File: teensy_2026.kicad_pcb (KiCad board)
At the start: 2 copper layers, 24.5 x 18 mm, 0 parts

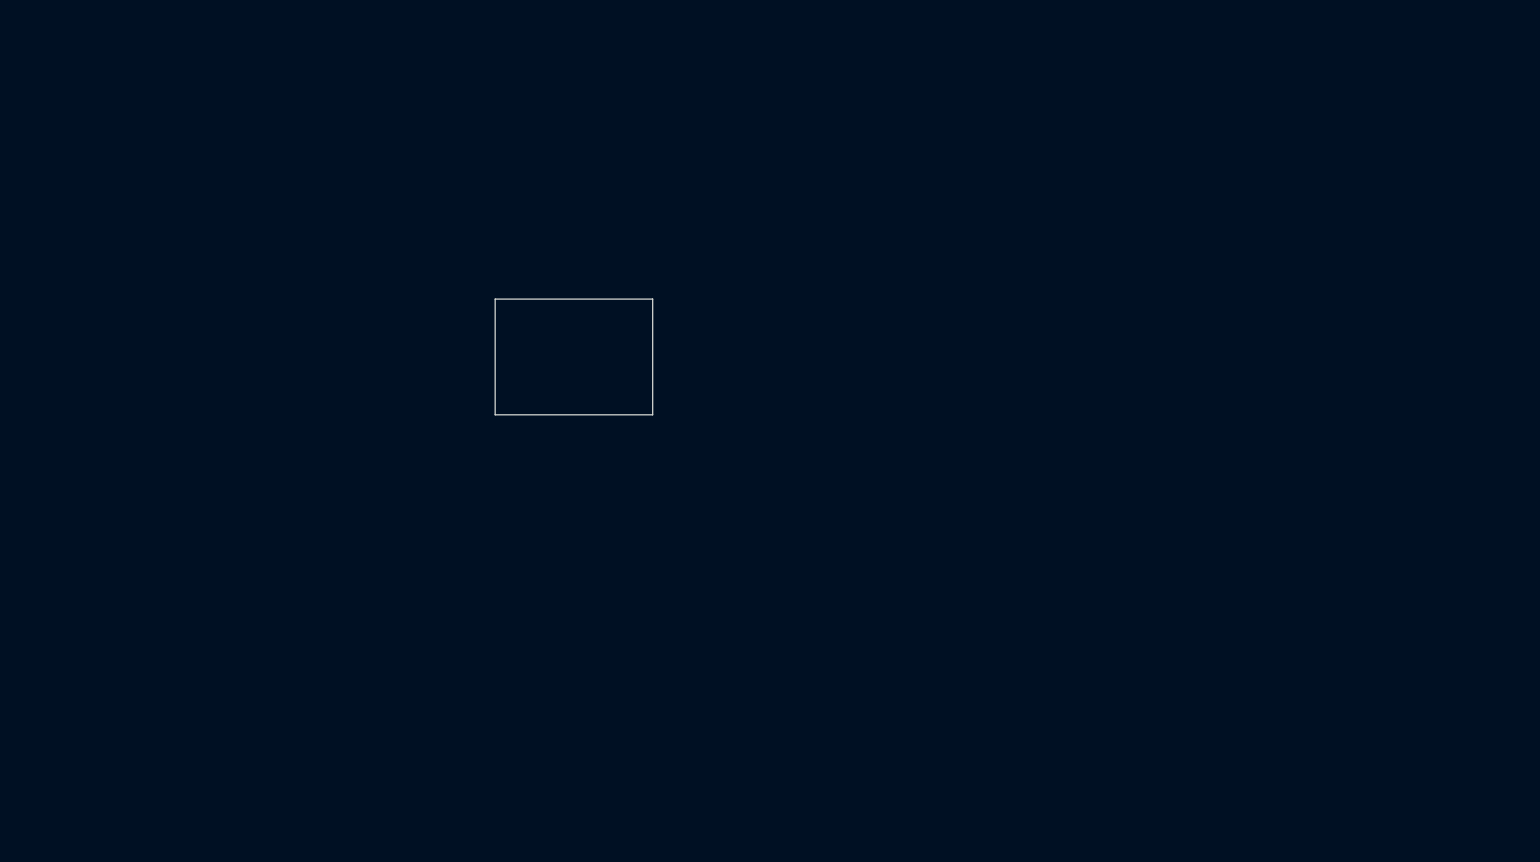
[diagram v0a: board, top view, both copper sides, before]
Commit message: started pcb layout
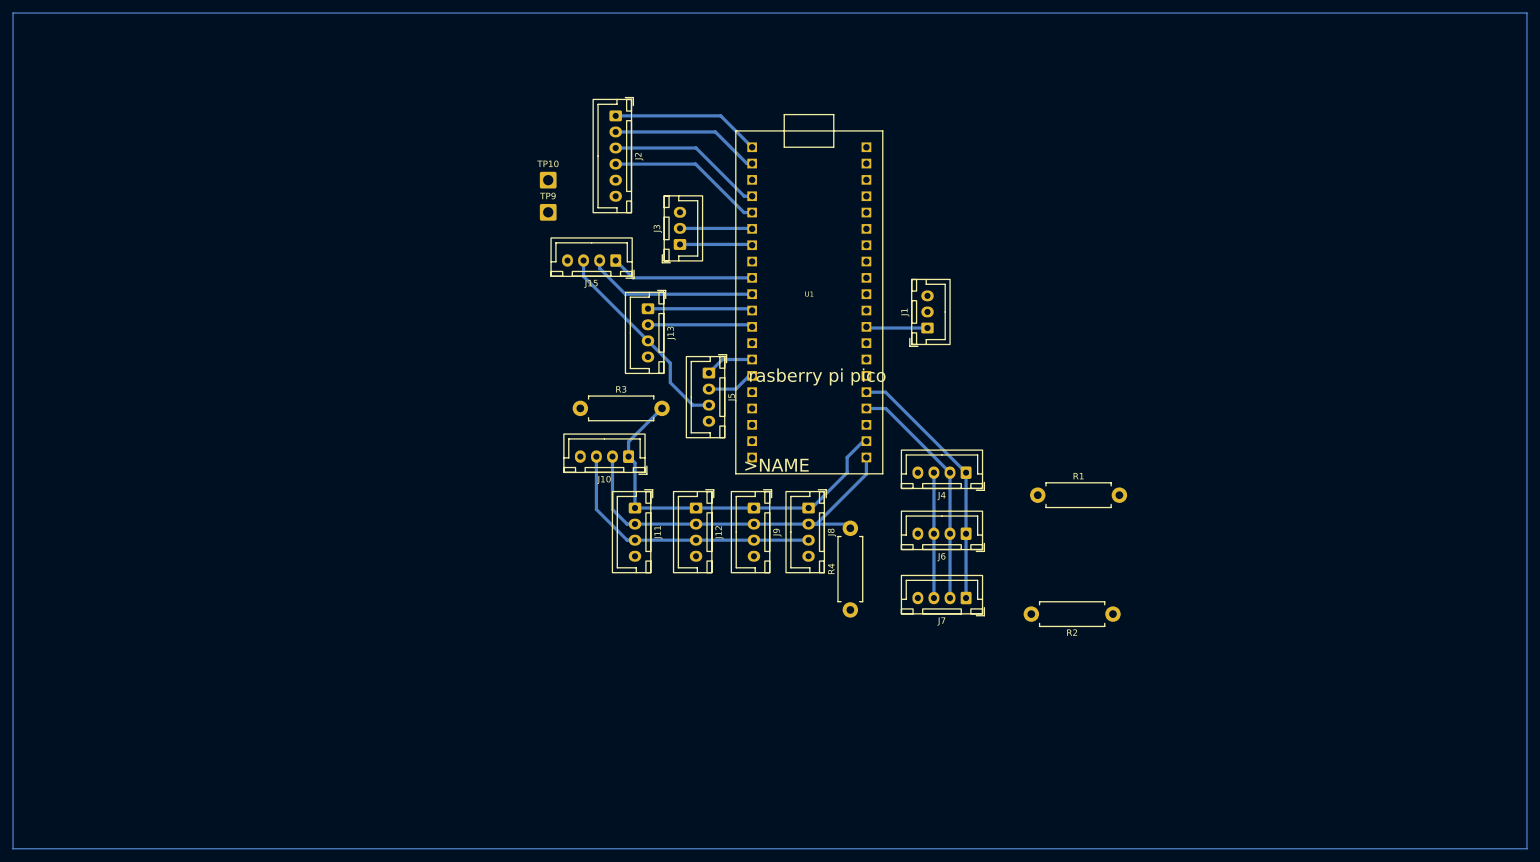
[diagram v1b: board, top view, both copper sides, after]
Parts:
- added J1: LED, Connector_JST:JST_XH_B3B-XH-A_1x03_P2.50mm_Vertical, F.Cu at (167.5, 69.5)
- added J10: Strain Gauge, Connector_JST:JST_XH_B4B-XH-A_1x04_P2.50mm_Vertical, F.Cu at (121.0, 89.5)
- added J11: Strain Gauge, Connector_JST:JST_XH_B4B-XH-A_1x04_P2.50mm_Vertical, F.Cu at (122.0, 97.5)
- added J12: Strain Gauge, Connector_JST:JST_XH_B4B-XH-A_1x04_P2.50mm_Vertical, F.Cu at (131.5, 97.5)
- added J13: UART 0 Placeholder, Connector_JST:JST_XH_B4B-XH-A_1x04_P2.50mm_Vertical, F.Cu at (124.0, 66.5)
- added J15: LinAct1, Connector_JST:JST_XH_B4B-XH-A_1x04_P2.50mm_Vertical, F.Cu at (119.0, 59.0)
- added J2: BattManagement, Connector_JST:JST_XH_B6B-XH-A_1x06_P2.50mm_Vertical, F.Cu at (119.0, 36.5)
- added J3: LinearActSaber, Connector_JST:JST_XH_B3B-XH-A_1x03_P2.50mm_Vertical, F.Cu at (129.0, 56.5)
- added J4: Current Sense, Connector_JST:JST_XH_B4B-XH-A_1x04_P2.50mm_Vertical, F.Cu at (173.5, 92.0)
- added J5: LinAct2, Connector_JST:JST_XH_B4B-XH-A_1x04_P2.50mm_Vertical, F.Cu at (133.5, 76.5)
- added J6: Current Sense, Connector_JST:JST_XH_B4B-XH-A_1x04_P2.50mm_Vertical, F.Cu at (173.5, 101.5)
- added J7: Current Sense, Connector_JST:JST_XH_B4B-XH-A_1x04_P2.50mm_Vertical, F.Cu at (173.5, 111.5)
- added J8: Strain Gauge, Connector_JST:JST_XH_B4B-XH-A_1x04_P2.50mm_Vertical, F.Cu at (149.0, 97.5)
- added J9: Strain Gauge, Connector_JST:JST_XH_B4B-XH-A_1x04_P2.50mm_Vertical, F.Cu at (140.5, 97.5)
- added R1: 10K, Resistor_THT:R_Axial_DIN0411_L9.9mm_D3.6mm_P12.70mm_Horizontal, F.Cu at (184.7, 95.5)
- added R2: 10K, Resistor_THT:R_Axial_DIN0411_L9.9mm_D3.6mm_P12.70mm_Horizontal, F.Cu at (196.3, 114.0)
- added R3: 10K, Resistor_THT:R_Axial_DIN0411_L9.9mm_D3.6mm_P12.70mm_Horizontal, F.Cu at (113.5, 82.0)
- added R4: 10K, Resistor_THT:R_Axial_DIN0411_L9.9mm_D3.6mm_P12.70mm_Horizontal, F.Cu at (155.5, 113.3)
- added TP10: LinAct TX TestPoint, Connector_Wire:SolderWire-0.75sqmm_1x01_D1.25mm_OD2.3mm, F.Cu at (108.5, 46.5)
- added TP9: LinAct RX TestPoint, Connector_Wire:SolderWire-0.75sqmm_1x01_D1.25mm_OD2.3mm, F.Cu at (108.5, 51.5)
- added U1: RASPBERRY_PI_PICO, pico:RASPBERRY_PI_PICO, F.Cu at (149.1, 64.2)
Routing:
- net +5V: track 0.00 -> 94.7 mm
- net /SDA 1: track 0.00 -> 61.2 mm
- net /SCL 1: track 0.00 -> 59.8 mm
- net /SCL 0: track 0.00 -> 40.2 mm
- net /SDA 0: track 0.00 -> 36.6 mm
- net /LA1_HE2_in: track 0.00 -> 26.6 mm
- net /BattManagement TX: track 0.00 -> 24.3 mm
- net /BattManagement SCK: track 0.00 -> 24.3 mm
- net /BattManagement CSn: track 0.00 -> 23.3 mm
- net /BattManagement RX: track 0.00 -> 23.2 mm
- net /LA1_HE1_in: track 0.00 -> 22.3 mm
- net /RX: track 0.00 -> 16.3 mm
- net /TX: track 0.00 -> 16.3 mm
- net /LinAct RX: track 0.00 -> 11.3 mm
- net /LinAct TX: track 0.00 -> 11.3 mm
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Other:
- board outline removed
